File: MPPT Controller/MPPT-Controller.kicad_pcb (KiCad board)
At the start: 4 copper layers, 95 parts, among them J1 Conn_01x02_Pin, J10 Conn_01x02_Pin, J2 Conn_01x02_Pin, J3 Conn_01x02_Pin, J4 Conn_01x02_Pin, J5 USB_C_Receptacle_USB2.0_16P, J6 Conn_01x02_Pin, J7 Conn_01x02_Pin, J8 Conn_01x02_Pin, J9 Conn_01x02_Pin, M1 Fan_4pin, Q1 IRL540N, SW1 SW_SPDT, U1 ADS1115IDGS, U2 ESP32-WROOM-32D, U3 CH340C, U4 LM1117DT-3.3, U5 LM2596S-ADJ, U6 TC4422, U7 ADS1115IDGS

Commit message: Wiring
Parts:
- moved JP1 0.51 mm to (95.2, 88.4)
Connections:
- U2 pad 14: unconnected-(U2-IO12-Pad14) -> RDY2
- U2 pad 31: RDY2 -> unconnected-(U2-IO19-Pad31)
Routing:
- net AmbientT: track 2.55 -> 103.6 mm, vias 0 -> 2
- net Aux1: track 7.96 -> 92.2 mm, vias 1 -> 2
- net RDY2: track 0.00 -> 74.6 mm, vias 0 -> 2
- net Net-(J10-Pin_2): track 0.00 -> 8.92 mm, vias 0 -> 1
- net Net-(J10-Pin_1): track 0.00 -> 8.89 mm, vias 0 -> 1
- net Aux2: track 0.00 -> 4.94 mm
- net PWM: track 76.1 -> 76.7 mm

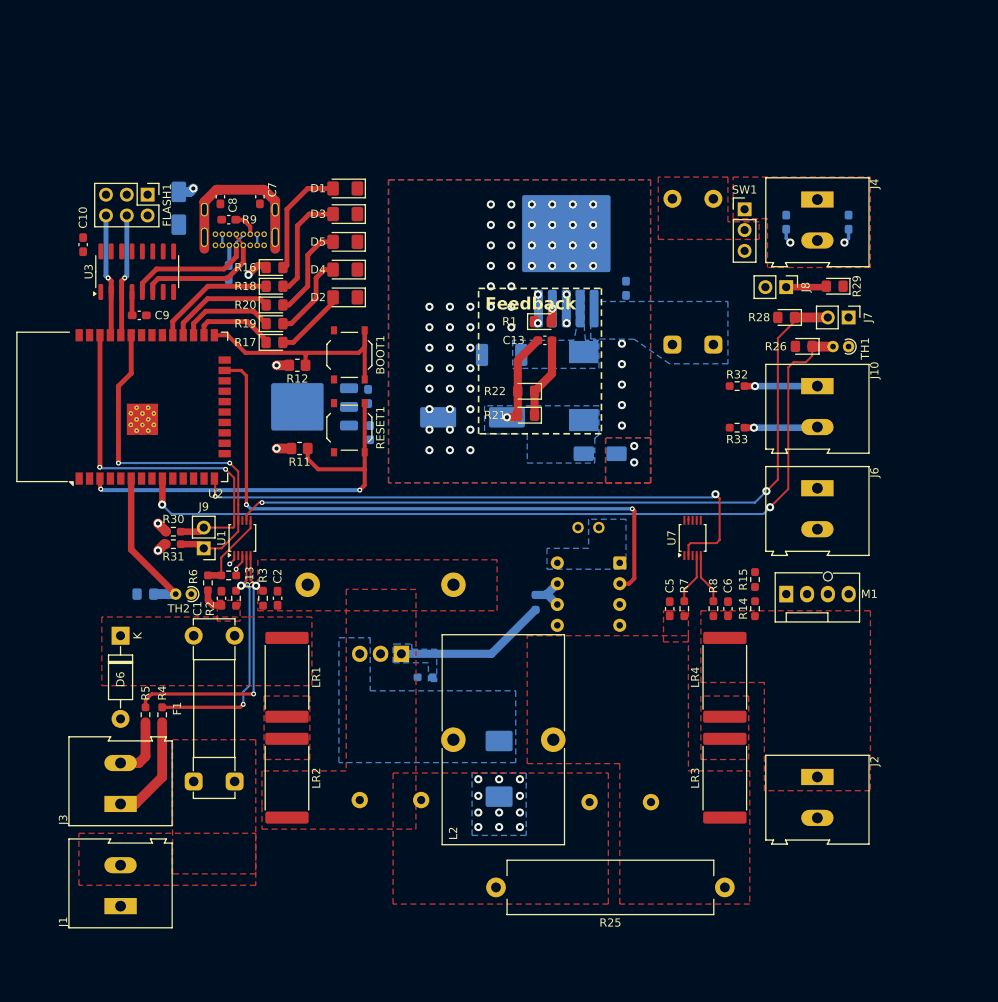
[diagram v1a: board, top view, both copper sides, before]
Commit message: Pin Swap Fan
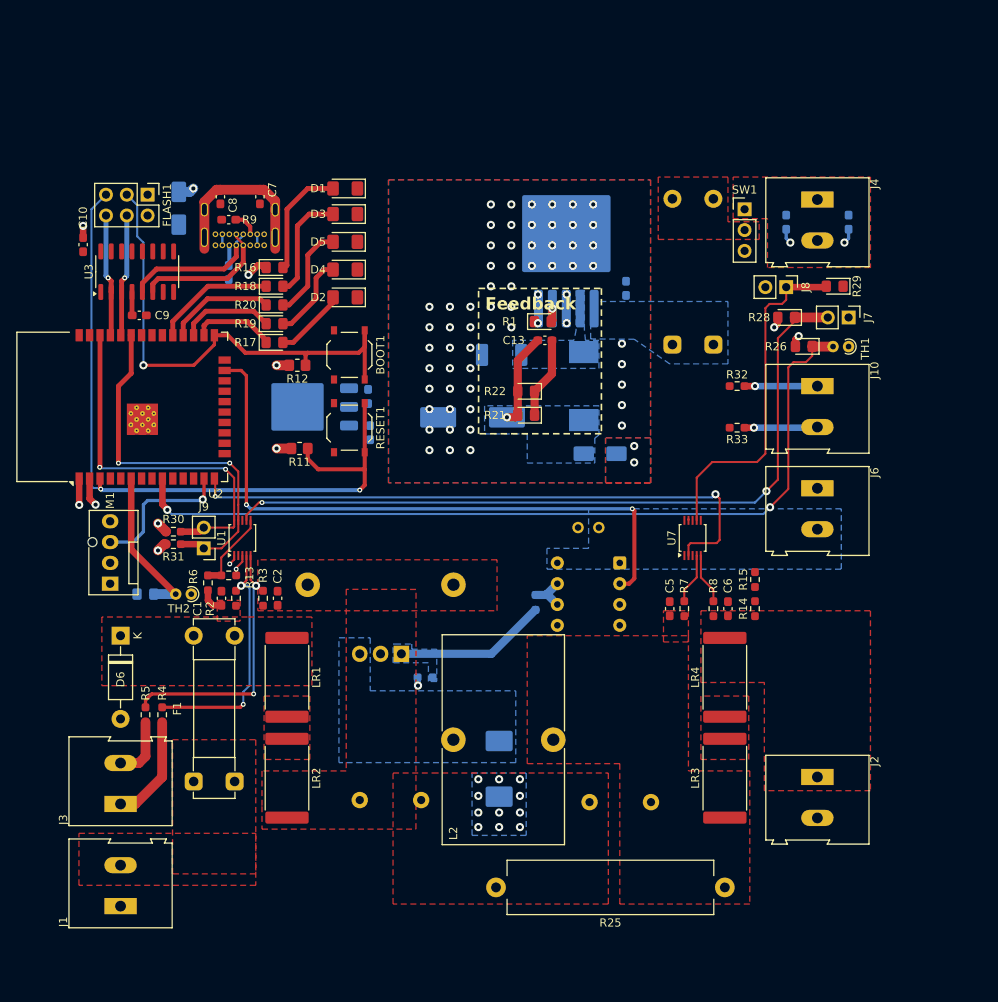
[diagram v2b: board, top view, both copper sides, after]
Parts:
- moved M1 82.6 mm to (35.6, 95.2), turned to 90 degrees
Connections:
- U2 pad 12: unconnected-(U2-IO27-Pad12) -> FanPWM
- U2 pad 16: FanPWM -> unconnected-(U2-IO13-Pad16)
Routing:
- net RST: track 52.6 -> 90.2 mm
- net Aux2: track 4.94 -> 42.0 mm
- net BOOT: track 29.2 -> 61.7 mm, vias 0 -> 1
- net Tacho: track 0.00 -> 18.2 mm, vias 0 -> 1
- net GND: track 2.73 -> 11.3 mm, vias 64 -> 69
- net +3V3: track 10.2 -> 13.7 mm, vias 6 -> 7

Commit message: DRC Run
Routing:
- net RDY1: track 0.00 -> 40.2 mm, vias 0 -> 2
- net OdiffA: track 6.21 -> 37.8 mm
- net OdiffB: track 6.21 -> 37.6 mm, vias 0 -> 2
- net FanPWM: track 0.00 -> 14.2 mm, vias 0 -> 1
- net RDY2: track 74.6 -> 80.9 mm
- net Net-(U5-FB): track 11.7 -> 16.6 mm
- net BOOT: track 61.7 -> 59.4 mm
- net VoltOut: track 0.00 -> 1.73 mm
- net Tacho: track 18.2 -> 17.5 mm
- net GND: vias 69 -> 68
- added copper zone on In2.Cu, net Vin

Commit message: SDA SCL Bus Route
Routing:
- net SDA: track 47.2 -> 109.1 mm, vias 2 -> 3
- net SCL: track 45.8 -> 105.9 mm, vias 2 -> 3
- net RDY2: track 80.9 -> 74.4 mm
- net RST: track 90.2 -> 92.8 mm
- net AmbientT: track 103.9 -> 105.3 mm
- net Aux1: track 92.2 -> 92.8 mm
- net Tacho: track 17.5 -> 18.0 mm

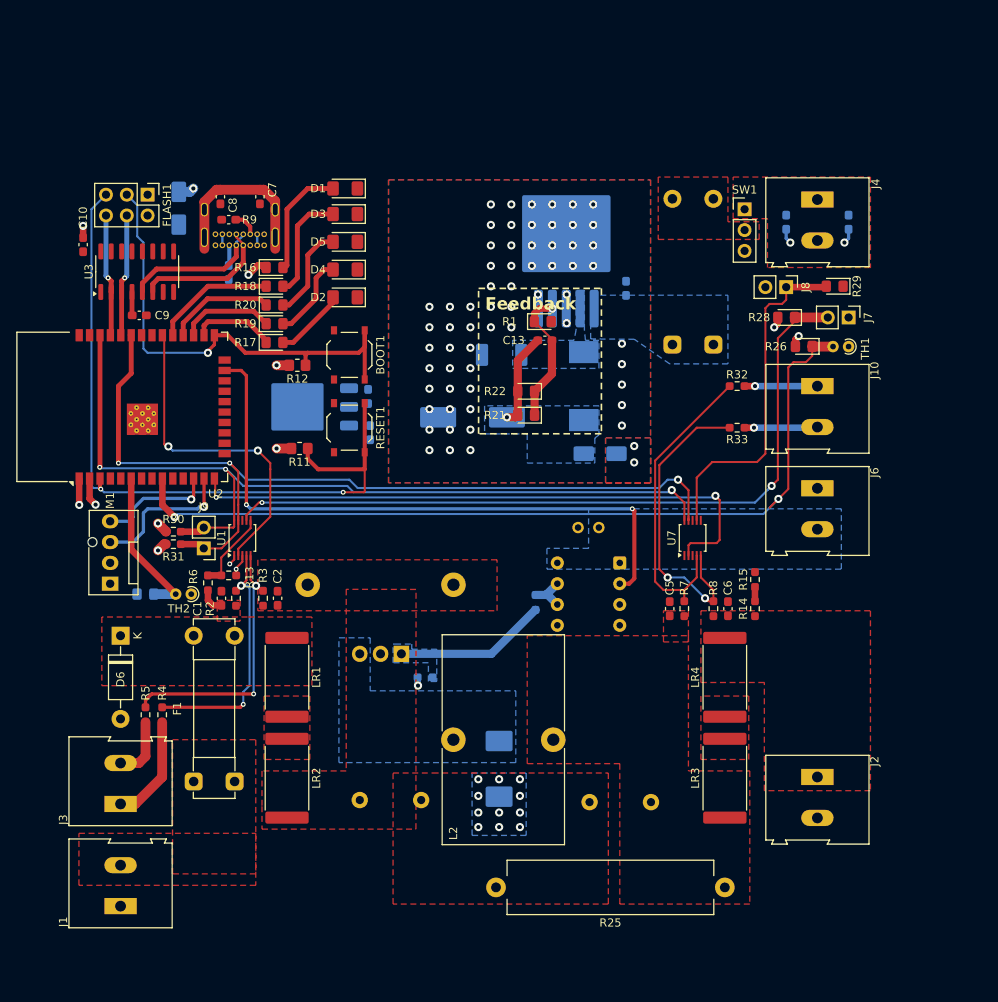
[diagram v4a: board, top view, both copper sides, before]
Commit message: Board Size 99x99mm
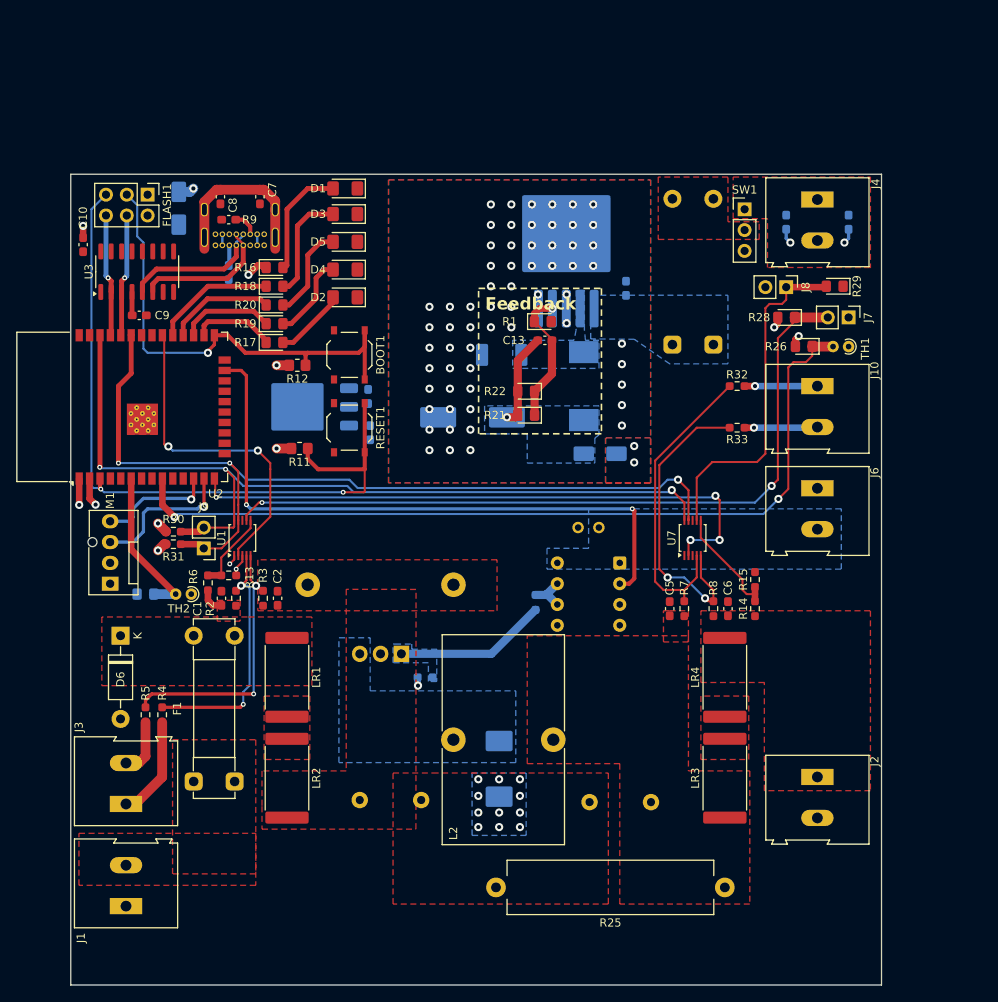
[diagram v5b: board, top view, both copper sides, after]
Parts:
- moved J1 0.67 mm to (37.5, 134.6)
- moved J3 0.67 mm to (37.5, 122.1)
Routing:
- net VoltOut: track 1.73 -> 14.1 mm
- net AmbientT: track 105.3 -> 103.8 mm
- net Aux1: track 92.8 -> 92.0 mm
- net RDY2: track 74.4 -> 74.6 mm, vias 2 -> 4
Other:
- board outline added: 99 x 99 mm
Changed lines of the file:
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@@
 	(footprint "TerminalBlock:TerminalBlock_Altech_AK300-2_P5.00mm"
 		(layer "F.Cu")
-		(at 36.83 122.145 90)
+		(at 37.5 122.145 90)
 		(descr "Altech AK300 terminal block, pitch 5.0mm, 45 degree angled, see http://www.mouser.com/ds/2/16/PCBMETRC-24178.pdf")
 		(tags "Altech AK300 terminal block pitch 5.0mm")
 		(property "Reference" "J3"
-			(at -1.92 -6.99 90)
+			(at 9.395 -5.75 90)
 			(layer "F.SilkS")
 			(effects
@@
 	(footprint "TerminalBlock:TerminalBlock_Altech_AK300-2_P5.00mm"
 		(layer "F.Cu")
-		(at 36.83 134.62 90)
+		(at 37.5 134.62 90)
 		(descr "Altech AK300 terminal block, pitch 5.0mm, 45 degree angled, see http://www.mouser.com/ds/2/16/PCBMETRC-24178.pdf")
 		(tags "Altech AK300 terminal block pitch 5.0mm")
 		(property "Reference" "J1"
-			(at -1.92 -6.99 90)
+			(at -3.88 -5.5 90)
 			(layer "F.SilkS")
 			(effects
@@
 		(layer "B.SilkS")
 	)
+	(gr_rect
+		(start 30.75 45.25)
+		(end 129.75 144.25)
+		(stroke
+			(width 0.05)
+			(type default)
+		)
+		(fill no)
+		(layer "Edge.Cuts")
+	)
 	(gr_text "Feedback"
 		(at 81.35 61.94 0)
@@
 	)
 	(segment
-		(start 114.3 95.6545)
+		(start 107.68 87.512)
+		(end 107.68 89.646)
+		(width 0.25)
+		(layer "F.Cu")
+		(net 44)
+	)
+	(segment
+		(start 112.776 96.012)
+		(end 113.284 96.52)
+		(width 0.25)
+		(layer "F.Cu")
+		(net 44)
+	)
+	(segment
+		(start 114.3 96.52)
 		(end 114.3 97.3855)
 		(width 0.8)
@@
 	)
 	(segment
+		(start 107.68 89.646)
+		(end 112.776 94.742)
+		(width 0.25)
+		(layer "F.Cu")
+		(net 44)
+	)
+	(segment
+		(start 114.3 95.6545)
+		(end 114.3 96.52)
+		(width 0.8)
+		(layer "F.Cu")
+		(net 44)
+	)
+	(segment
+		(start 112.776 94.742)
+		(end 112.776 96.012)
+		(width 0.25)
+		(layer "F.Cu")
+		(net 44)
+	)
+	(segment
+		(start 113.284 96.52)
+		(end 114.3 96.52)
+		(width 0.25)
+		(layer "F.Cu")
+		(net 44)
+	)
+	(segment
 		(start 47.498 63.246)
 		(end 47.02 63.724)
@@
 	(segment
 		(start 116.332 83.312)
-		(end 115.824 83.82)
-		(width 0.25)
-		(layer "B.Cu")
-		(net 50)
-	)
-	(segment
-		(start 116.332 83.312)
 		(end 114.3 85.344)
 		(width 0.25)
@@
 	)
 	(segment
-		(start 116.078 85.979)
-		(end 117.1575 84.8995)
-		(width 0.25)
-		(layer "F.Cu")
-		(net 61)
-	)
-	(segment
 		(start 118.364 68.834)
 		(end 118.999 68.199)
@@
 	)
 	(segment
-		(start 109.982 89.916)
-		(end 109.601 90.297)
+		(start 109.982 85.027)
+		(end 109.982 89.916)
 		(width 0.25)
 		(layer "F.Cu")
@@
 	)
 	(segment
-		(start 109.474 84.519)
-		(end 109.982 85.027)
+		(start 106.426 89.916)
+		(end 106.18 90.162)
 		(width 0.25)
 		(layer "F.Cu")
@@
 	)
 	(segment
-		(start 48.514 84.709)
-		(end 48.387 84.582)
+		(start 109.474 84.519)
+		(end 109.982 85.027)
 		(width 0.25)
 		(layer "F.Cu")
@@
 	)
 	(segment
-		(start 106.18 90.543)
-		(end 106.18 91.812)
+		(start 48.514 84.709)
+		(end 48.387 84.582)
 		(width 0.25)
 		(layer "F.Cu")
@@
 	)
 	(segment
-		(start 109.982 85.027)
-		(end 109.982 89.916)
+		(start 106.18 90.162)
+		(end 106.18 91.812)
 		(width 0.25)
 		(layer "F.Cu")
 		(net 88)
 	)
-	(segment
-		(start 106.426 90.297)
-		(end 106.18 90.543)
-		(width 0.25)
-		(layer "F.Cu")
+	(via
+		(at 48.514 84.709)
+		(size 0.6)
+		(drill 0.3)
+		(layers "F.Cu" "B.Cu")
 		(net 88)
 	)
-	(segment
-		(start 109.601 90.297)
-		(end 106.426 90.297)
-		(width 0.25)
-		(layer "F.Cu")
+	(via
+		(at 106.426 89.916)
+		(size 1)
+		(drill 0.5)
+		(layers "F.Cu" "B.Cu")
 		(net 88)
 	)
 	(via
-		(at 48.514 84.709)
-		(size 0.6)
-		(drill 0.3)
+		(at 109.982 89.916)
+		(size 1)
+		(drill 0.5)
 		(layers "F.Cu" "B.Cu")
 		(net 88)
@@
 		(net 88)
 	)
+	(segment
+		(start 109.982 89.916)
+		(end 106.426 89.916)
+		(width 0.25)
+		(layer "B.Cu")
+		(net 88)
+	)

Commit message: Ground Fill
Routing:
- net +3V3: track 13.7 -> 30.5 mm, vias 7 -> 10
- net GND: track 11.3 -> 27.8 mm, vias 68 -> 73
- net +5V: track 0.00 -> 8.79 mm, vias 2 -> 5
- net RST: track 92.8 -> 94.9 mm
- net RDY1: track 40.2 -> 41.4 mm
- net VoltIn: track 9.83 -> 10.6 mm
- added copper zone on B.Cu, net +3V3
- added copper zone on In2.Cu, net +5V
- removed copper zone on B.Cu, net +5V
- removed copper zone on F.Cu, net +5V

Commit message: First Draft
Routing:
- net GND: track 27.8 -> 36.9 mm, vias 73 -> 77
- net +5V: track 8.79 -> 13.9 mm
- net Vin: vias 0 -> 1
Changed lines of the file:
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@@
 	)
 	(via
+		(at 64.75 70.5)
+		(size 1)
+		(drill 0.5)
+		(layers "F.Cu" "B.Cu")
+		(free yes)
+		(net 2)
+	)
+	(via
+		(at 37.75 97.25)
+		(size 1)
+		(drill 0.5)
+		(layers "F.Cu" "B.Cu")
+		(free yes)
+		(net 2)
+	)
+	(via
 		(at 89.55 51.44)
 		(size 1)
@@
 	)
 	(via
+		(at 49.149 96.1655)
+		(size 1)
+		(drill 0.5)
+		(layers "F.Cu" "B.Cu")
+		(net 2)
+	)
+	(via
 		(at 77.05 66.44)
 		(size 1)
@@
 	)
 	(via
+		(at 56.007 96.1655)
+		(size 1)
+		(drill 0.5)
+		(layers "F.Cu" "B.Cu")
+		(net 2)
+	)
+	(via
 		(at 104 92.25)
 		(size 1)
@@
 	)
 	(segment
+		(start 50.038 58.113)
+		(end 49.363 58.113)
+		(width 0.6)
+		(layer "B.Cu")
+		(net 2)
+	)
+	(segment
+		(start 67.056 71.5275)
+		(end 64.8775 71.5275)
+		(width 1)
+		(layer "B.Cu")
+		(net 2)
+	)
+	(segment
+		(start 37.75 97.25)
+		(end 38.114 97.25)
+		(width 1)
+		(layer "B.Cu")
+		(net 2)
+	)
+	(segment
+		(start 48.416 57.166)
+		(end 48.416 53.928)
+		(width 0.6)
+		(layer "B.Cu")
+		(net 2)
+	)
+	(segment
+		(start 49.363 58.113)
+		(end 48.416 57.166)
+		(width 0.6)
+		(layer "B.Cu")
+		(net 2)
+	)
+	(segment
 		(start 73.105 106.68)
 		(end 73.105 107.649)
@@
 	)
 	(segment
+		(start 64.8775 71.5275)
+		(end 64.73 71.38)
+		(width 1)
+		(layer "B.Cu")
+		(net 2)
+	)
+	(segment
+		(start 38.114 97.25)
+		(end 38.844 96.52)
+		(width 1)
+		(layer "B.Cu")
+		(net 2)
+	)
+	(segment
 		(start 73.152 107.696)
 		(end 73.105 107.649)
@@
 	)
 	(via
+		(at 50 98.5)
+		(size 1)
+		(drill 0.5)
+		(layers "F.Cu" "B.Cu")
+		(free yes)
+		(net 3)
+	)
+	(via
 		(at 125.222 53.594)
 		(size 1)
@@
 	)
 	(segment
+		(start 99.55 80.44)
+		(end 98.455 80.44)
+		(width 1.4)
+		(layer "B.Cu")
+		(net 10)
+	)
+	(segment
+		(start 98.325 78.44)
+		(end 97.39 79.375)
+		(width 1.4)
+		(layer "B.Cu")
+		(net 10)
+	)
+	(segment
 		(start 67.304 75.94)
 		(end 67.31 75.946)
@@
 	)
 	(segment
+		(start 98.455 80.44)
+		(end 97.39 79.375)
+		(width 1.4)
+		(layer "B.Cu")
+		(net 10)
+	)
+	(segment
+		(start 99.55 78.44)
+		(end 98.325 78.44)
+		(width 1.4)
+		(layer "B.Cu")
+		(net 10)
+	)
+	(segment
 		(start 92.696 88.392)
 		(end 92.696 87.054)
@@
 		(layer "F.Cu")
 		(hatch edge 0.5)
-		(priority 4)
+		(priority 17)
 		(connect_pads
 			(clearance 0.5)
@@
 		(layer "F.Cu")
 		(hatch edge 0.5)
-		(priority 3)
+		(priority 15)
 		(connect_pads thru_hole_only
 			(clearance 0.7)
@@
 		(layer "B.Cu")
 		(hatch edge 0.5)
-		(priority 6)
+		(priority 55)
 		(connect_pads thru_hole_only
 			(clearance 0.5)
@@
 		(layer "B.Cu")
 		(hatch edge 0.5)
-		(priority 17)
+		(priority 80)
 		(connect_pads yes
 			(clearance 0.8)
@@
 		(layer "B.Cu")
 		(hatch edge 0.5)
-		(priority 9)
+		(priority 75)
 		(connect_pads yes
 			(clearance 1)
@@
 		(polygon
 			(pts
-				(xy 63.5 101.854) (xy 67.31 101.854) (xy 67.31 108.331) (xy 85.09 108.331) (xy 85.09 117.094) (xy 63.5 117.094)
+				(xy 63.5 101.854) (xy 67.31 101.854) (xy 67.31 110.831) (xy 85.09 110.831) (xy 85.09 117.094) (xy 63.5 117.094)
 				(xy 63.5 107.696)
 			)
@@
 		(polygon
 			(pts
-				(xy 31 45.25) (xy 69.5 45.25) (xy 69.55 87.5) (xy 106.5 87.5) (xy 106.5 60.5) (xy 129 60.5) (xy 129 112.75)
-				(xy 31 112.75)
+				(xy 31 45.25) (xy 69.5 45.25) (xy 69.55 87.5) (xy 106.5 87.5) (xy 106.5 60.5) (xy 129 60.5) (xy 129 128.75)
+				(xy 31 128.75)
 			)
 		)

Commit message: Silk Block Diagram
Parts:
- added G***: LOGO, LOGO, F.Cu at (129.1, 120.3)
- added J11: Conn_01x02_Pin, Connector_PinSocket_2.54mm:PinSocket_2x01_P2.54mm_Vertical, F.Cu at (65.6, 51.9)
- moved J8 22.8 mm to (130.4, 39.8)
- moved R28 22.8 mm to (130.4, 43.5)
- moved C15 22.8 mm to (92.1, 55.7)
- moved C2 22.8 mm to (68.3, 77.8)
- moved C4 22.8 mm to (130.4, 31.9)
- moved L1 22.8 mm to (105.6, 51.9)
- moved LR1 22.8 mm to (69.4, 87.4)
- moved LR2 22.8 mm to (69.4, 99.8)
- moved R16 22.8 mm to (67.9, 37.4)
- moved R17 22.8 mm to (67.9, 46.5)
- moved R18 22.8 mm to (67.9, 39.7)
- moved R19 22.8 mm to (67.9, 44.2)
- moved R20 22.8 mm to (67.9, 42.0)
- moved R32 22.8 mm to (124.4, 51.9)
- moved BOOT1 22.8 mm to (77.0, 48.1)
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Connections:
- U2 pad 16: unconnected-(U2-IO13-Pad16) -> PWM
- U2 pad 23: PWM -> USR1
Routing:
- net PWM: track 76.7 -> 67.5 mm
- net USR1: track 0.00 -> 4.59 mm
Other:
- outline, holes or cut-outs redrawn
- board text added: "+"
- board text added: "220 Ohm 0805"
- board text added: "2x 0.1 Ohm 4020 Shunt"
- board text added: "3.3V"
- board text added: "Aux V Input"
- board text added: "BOOT"
- board text added: "Beat"
- board text added: "C16 Buffer Capacitor"
- board text added: "C17 Buffer Capacitor"
- board text added: "CH340C"
- board text added: "Charge"
- board text added: "FET - Supply +"
- board text added: "FET AUX Supply"
- board text added: "Fault!"
- board text added: "Fuse 10A 5x20mm"
- board text added: "GPIO15"
- board text added: "Inductor Coil"
- board text added: "Input"
- board text added: "MPPT"
- board text added: "Measure"
- board text added: "Output"
- board text added: "Output A Shunt B"
- board text added: "Output I Shunt"
- board text added: "R25"
- board text added: "RESET"
- board text added: "Reverse Diode"
- board text added: "TO220 N MOSFET"
- board text added: "Vaux - +"
- board text added: "Vaux SPDT Vin"
- board text added: "WayWayWay"
